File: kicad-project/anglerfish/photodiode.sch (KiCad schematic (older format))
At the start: 5 parts, among them U1 APDS-9306-065

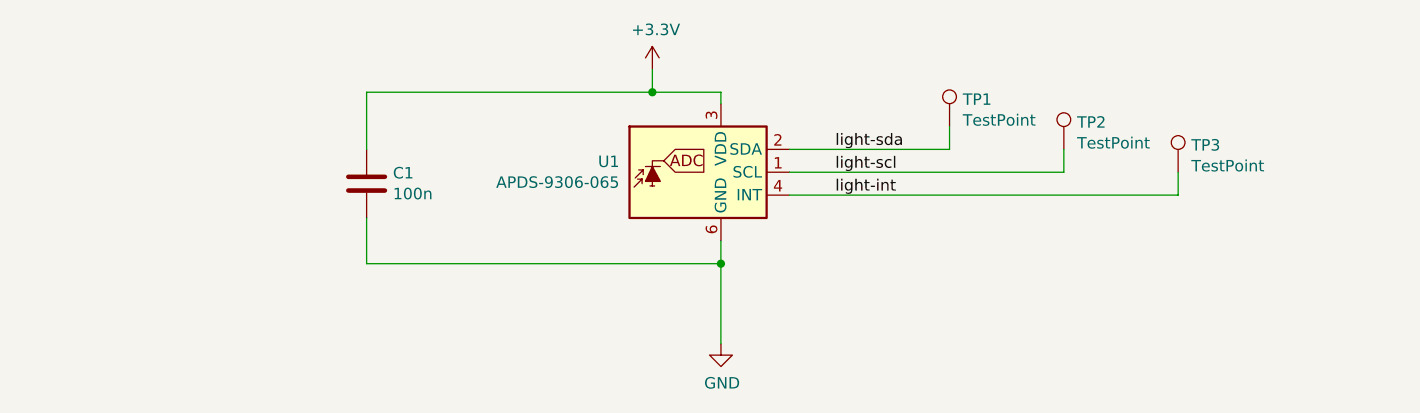
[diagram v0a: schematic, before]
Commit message: Schematic entered. Adding placing the resistors in the layout now.
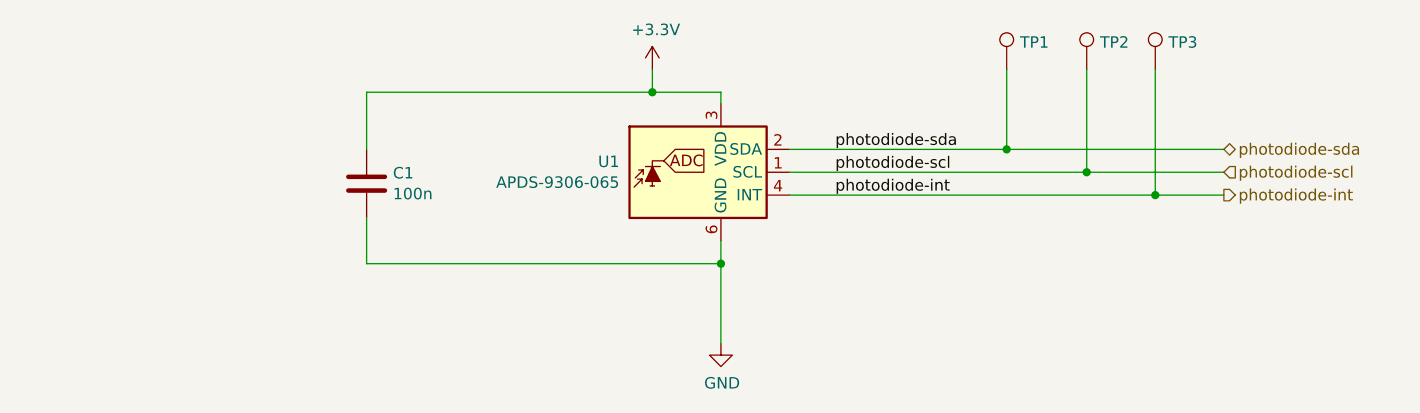
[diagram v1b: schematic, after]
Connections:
- net light-int renamed photodiode-int
- net light-scl renamed photodiode-scl
- net light-sda renamed photodiode-sda
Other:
- moved on the sheet: TP1, TP2, TP3
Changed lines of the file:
@@
 $Descr A4 11693 8268
 encoding utf-8
-Sheet 2 2
+Sheet 2 3
 Title "Anglerfish"
 Date "2020-05-10"
@@
 L Connector:TestPoint TP?
 U 1 1 5DD2446E
-P 6600 3300
+P 6850 3050
 AR Path="/5DD2446E" Ref="TP?"  Part="1"
 AR Path="/5D7D4F90/5DD2446E" Ref="TP?"  Part="1"
@@
 AR Path="/5DD1C388/5DD2446E" Ref="TP?"  Part="1"
 AR Path="/5FEEB7E0/5DD2446E" Ref="TP1"  Part="1"
-F 0 "TP1" H 6658 3418 50  0000 L CNN
-F 1 "TestPoint" H 6658 3327 50  0000 L CNN
-F 2 "TestPoint:TestPoint_Pad_D1.5mm" H 6800 3300 50  0001 C CNN
-F 3 "~" H 6800 3300 50  0001 C CNN
-	1    6600 3300
+F 0 "TP1" H 6908 3168 50  0000 L CNN
+F 1 "TestPoint" H 6908 3077 50  0001 L CNN
+F 2 "TestPoint:TestPoint_Pad_D1.5mm" H 7050 3050 50  0001 C CNN
+F 3 "~" H 7050 3050 50  0001 C CNN
+	1    6850 3050
 	1    0    0    -1
 $EndComp
-Wire Wire Line
-	6600 3400 6600 3300
 $Comp
 L Connector:TestPoint TP?
 U 1 1 5DD2470C
-P 7100 3400
+P 7200 3050
 AR Path="/5DD2470C" Ref="TP?"  Part="1"
 AR Path="/5D7D4F90/5DD2470C" Ref="TP?"  Part="1"
@@
 AR Path="/5DD1C388/5DD2470C" Ref="TP?"  Part="1"
 AR Path="/5FEEB7E0/5DD2470C" Ref="TP2"  Part="1"
-F 0 "TP2" H 7158 3518 50  0000 L CNN
-F 1 "TestPoint" H 7158 3427 50  0000 L CNN
-F 2 "TestPoint:TestPoint_Pad_D1.5mm" H 7300 3400 50  0001 C CNN
-F 3 "~" H 7300 3400 50  0001 C CNN
-	1    7100 3400
+F 0 "TP2" H 7258 3168 50  0000 L CNN
+F 1 "TestPoint" H 7258 3077 50  0001 L CNN
+F 2 "TestPoint:TestPoint_Pad_D1.5mm" H 7400 3050 50  0001 C CNN
+F 3 "~" H 7400 3050 50  0001 C CNN
+	1    7200 3050
 	1    0    0    -1
 $EndComp
-Wire Wire Line
-	7100 3500 7100 3400
-$Comp
-L Connector:TestPoint TP?
-U 1 1 5DD24ABF
-P 7600 3500
-AR Path="/5DD24ABF" Ref="TP?"  Part="1"
-AR Path="/5D7D4F90/5DD24ABF" Ref="TP?"  Part="1"
-AR Path="/5D841DAD/5DD24ABF" Ref="TP?"  Part="1"
-AR Path="/5D930A7F/5DD24ABF" Ref="TP?"  Part="1"
-AR Path="/5D9AC14C/5DD24ABF" Ref="TP?"  Part="1"
-AR Path="/5D9CE382/5DD24ABF" Ref="TP?"  Part="1"
-AR Path="/5DD1C388/5DD24ABF" Ref="TP?"  Part="1"
-AR Path="/5FEEB7E0/5DD24ABF" Ref="TP3"  Part="1"
-F 0 "TP3" H 7658 3618 50  0000 L CNN
-F 1 "TestPoint" H 7658 3527 50  0000 L CNN
-F 2 "TestPoint:TestPoint_Pad_D1.5mm" H 7800 3500 50  0001 C CNN
-F 3 "~" H 7800 3500 50  0001 C CNN
-	1    7600 3500
-	1    0    0    -1
-$EndComp
-Wire Wire Line
-	7600 3600 7600 3500
 $Comp
 L Device:C C1
@@
 Wire Wire Line
 	4050 3150 4050 3400
-Wire Wire Line
-	5900 3400 6600 3400
-Wire Wire Line
-	5900 3500 7100 3500
-Wire Wire Line
-	5900 3600 7600 3600
 Text Label 6100 3400 0    50   ~ 0
-light-sda
+photodiode-sda
 Text Label 6100 3500 0    50   ~ 0
-light-scl
+photodiode-scl
 Text Label 6100 3600 0    50   ~ 0
-light-int
+photodiode-int
 $Comp
 L power:GND #PWR02
@@
 Wire Wire Line
 	5600 3900 5600 4250
+$Comp
+L Connector:TestPoint TP?
+U 1 1 5DD24ABF
+P 7500 3050
+AR Path="/5DD24ABF" Ref="TP?"  Part="1"
+AR Path="/5D7D4F90/5DD24ABF" Ref="TP?"  Part="1"
+AR Path="/5D841DAD/5DD24ABF" Ref="TP?"  Part="1"
+AR Path="/5D930A7F/5DD24ABF" Ref="TP?"  Part="1"
+AR Path="/5D9AC14C/5DD24ABF" Ref="TP?"  Part="1"
+AR Path="/5D9CE382/5DD24ABF" Ref="TP?"  Part="1"
+AR Path="/5DD1C388/5DD24ABF" Ref="TP?"  Part="1"
+AR Path="/5FEEB7E0/5DD24ABF" Ref="TP3"  Part="1"
+F 0 "TP3" H 7558 3168 50  0000 L CNN
+F 1 "TestPoint" H 7558 3077 50  0001 L CNN
+F 2 "TestPoint:TestPoint_Pad_D1.5mm" H 7700 3050 50  0001 C CNN
+F 3 "~" H 7700 3050 50  0001 C CNN
+	1    7500 3050
+	1    0    0    -1
+$EndComp
+Text HLabel 7800 3400 2    50   BiDi ~ 0
+photodiode-sda
+Text HLabel 7800 3500 2    50   Input ~ 0
+photodiode-scl
+Text HLabel 7800 3600 2    50   Output ~ 0
+photodiode-int
+Wire Wire Line
+	5900 3600 7500 3600
+Wire Wire Line
+	5900 3500 7200 3500
+Wire Wire Line
+	5900 3400 6850 3400
+Wire Wire Line
+	6850 3050 6850 3400
+Connection ~ 6850 3400
+Wire Wire Line
+	6850 3400 7800 3400
+Wire Wire Line
+	7200 3050 7200 3500
+Connection ~ 7200 3500
+Wire Wire Line
+	7200 3500 7800 3500
+Wire Wire Line
+	7500 3050 7500 3600
+Connection ~ 7500 3600
+Wire Wire Line
+	7500 3600 7800 3600
 $EndSCHEMATC

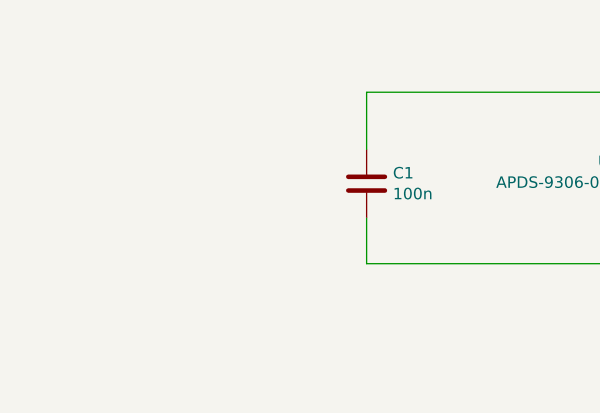
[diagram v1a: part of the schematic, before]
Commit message: Generated gerbers. I discovered that I was working in a temp folder, so I erased the files under the anglerfish folder and manually brought the files from the temp folder.
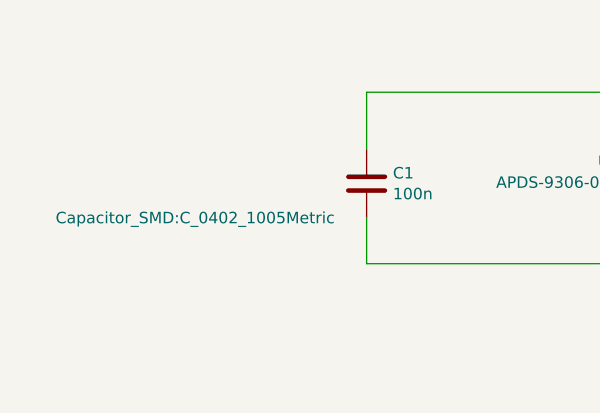
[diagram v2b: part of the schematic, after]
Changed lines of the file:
@@
 F 0 "C1" H 4165 3596 50  0000 L CNN
 F 1 "100n" H 4165 3505 50  0000 L CNN
-F 2 "Capacitor_SMD:C_0402_1005Metric" H 4088 3400 50  0001 C CNN
+F 2 "Capacitor_SMD:C_0402_1005Metric" H 3300 3400 50  0000 C CNN
 F 3 "~" H 4050 3550 50  0001 C CNN
 	1    4050 3550
